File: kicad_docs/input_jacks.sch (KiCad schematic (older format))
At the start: 32 parts, among them J10 gate_3_in, J11 trigger_3_in, J12 gate_4_in, J13 trigger_4_in, J6 gate_1_i n, J7 trigger_1_in, J8 gate_2_in, J9 trigger_2_in, Q10 MMBT3904, Q11 MMBT3904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

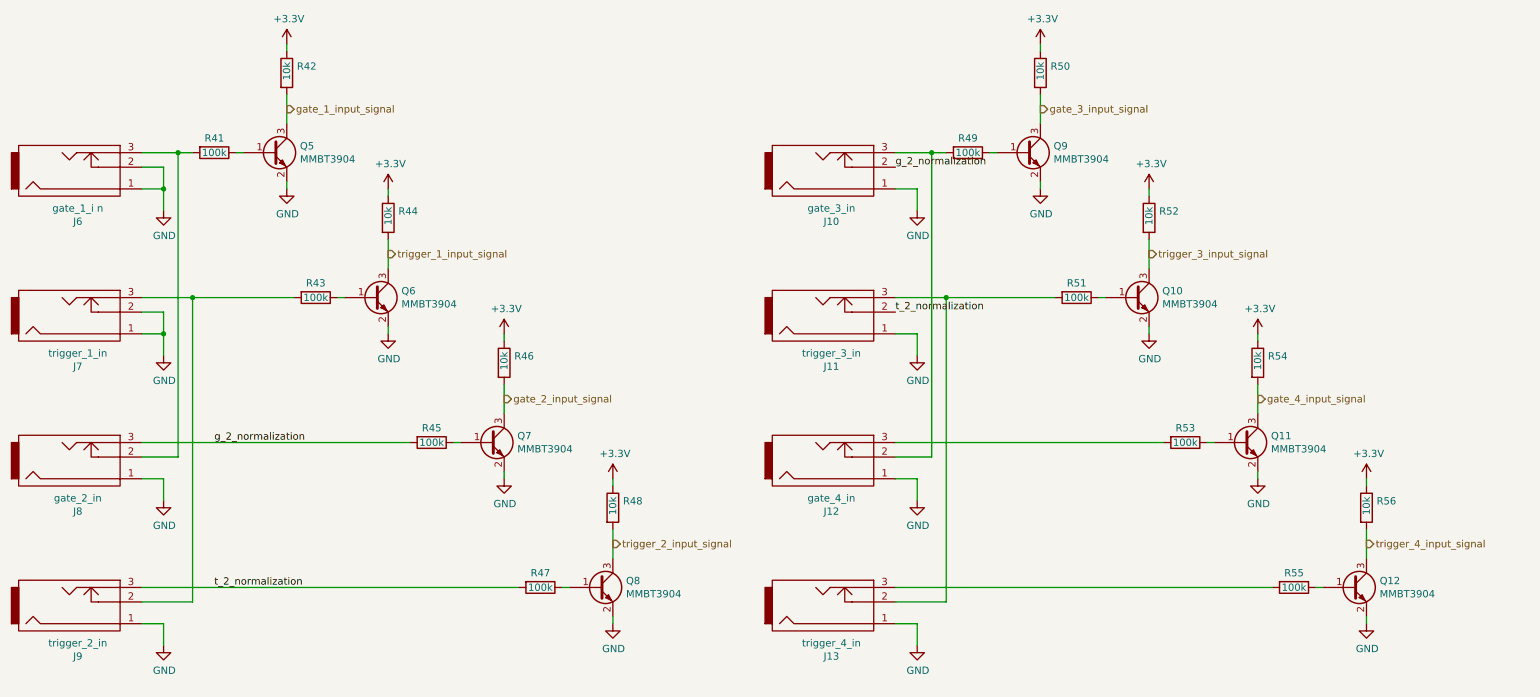
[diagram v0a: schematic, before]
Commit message: add EEPROM, big pcb re-design
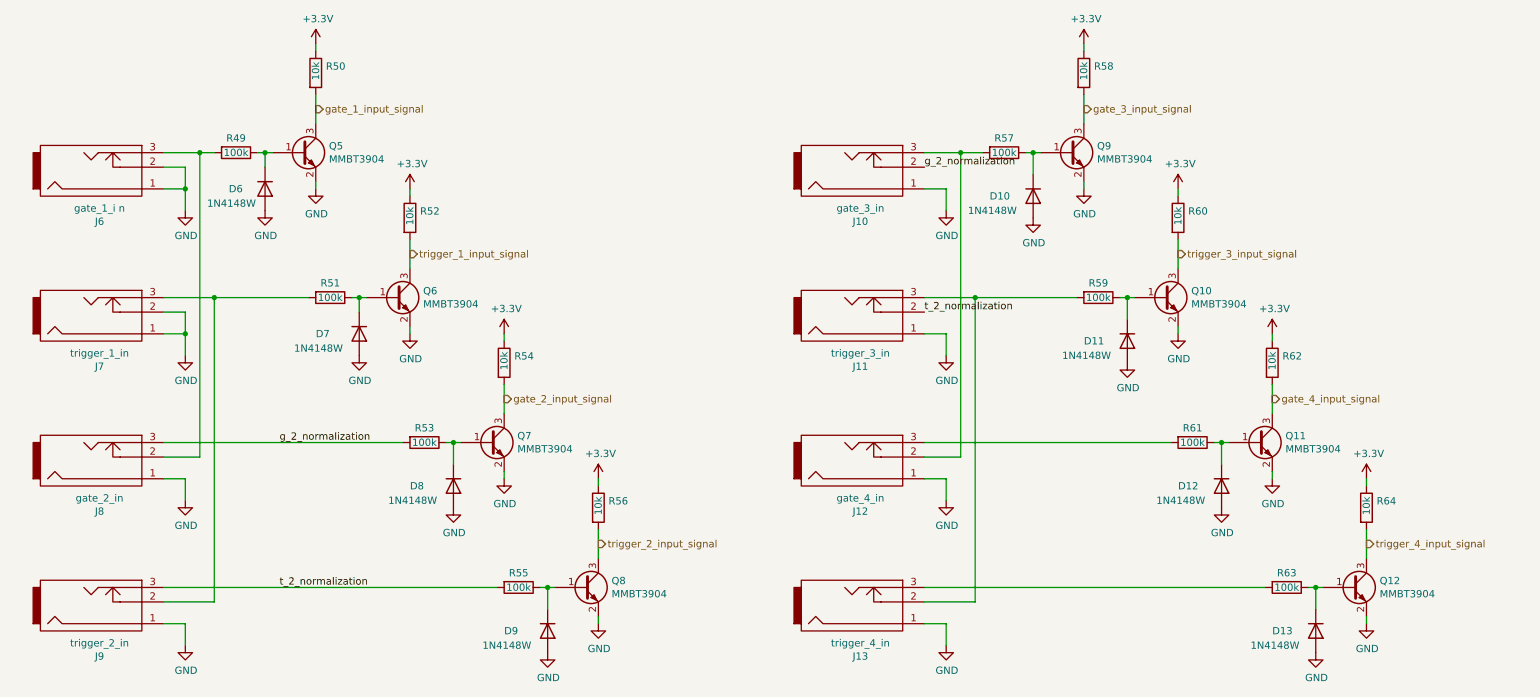
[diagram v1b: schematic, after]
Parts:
- added D10, D11, D12, D13, D6, D7, D8, D9: 1N4148W, Diode_SMD:D_SOD-123, symbol Diode:1N4148W
- Q10, Q11, Q12, Q5, Q6, Q7, Q8, Q9: footprint Package_TO_SOT_SMD:SOT-23_Handsoldering -> Package_TO_SOT_SMD:SOT-23
- R49: renamed from R41; footprint Resistor_SMD:R_0805_2012Metric_Pad1.15x1.40mm_HandSolder -> Resistor_SMD:R_0603_1608Metric
- R50: renamed from R42; footprint Resistor_SMD:R_0805_2012Metric_Pad1.15x1.40mm_HandSolder -> Resistor_SMD:R_0603_1608Metric
- R51: renamed from R43; footprint Resistor_SMD:R_0805_2012Metric_Pad1.15x1.40mm_HandSolder -> Resistor_SMD:R_0603_1608Metric
- R52: renamed from R44; footprint Resistor_SMD:R_0805_2012Metric_Pad1.15x1.40mm_HandSolder -> Resistor_SMD:R_0603_1608Metric
- R53: renamed from R45; footprint Resistor_SMD:R_0805_2012Metric_Pad1.15x1.40mm_HandSolder -> Resistor_SMD:R_0603_1608Metric
- R54: renamed from R46; footprint Resistor_SMD:R_0805_2012Metric_Pad1.15x1.40mm_HandSolder -> Resistor_SMD:R_0603_1608Metric
- R55: renamed from R47; footprint Resistor_SMD:R_0805_2012Metric_Pad1.15x1.40mm_HandSolder -> Resistor_SMD:R_0603_1608Metric
- R56: renamed from R48; footprint Resistor_SMD:R_0805_2012Metric_Pad1.15x1.40mm_HandSolder -> Resistor_SMD:R_0603_1608Metric
- R57: renamed from R49; footprint Resistor_SMD:R_0805_2012Metric_Pad1.15x1.40mm_HandSolder -> Resistor_SMD:R_0603_1608Metric
- R58: renamed from R50; footprint Resistor_SMD:R_0805_2012Metric_Pad1.15x1.40mm_HandSolder -> Resistor_SMD:R_0603_1608Metric
- R59: renamed from R51; footprint Resistor_SMD:R_0805_2012Metric_Pad1.15x1.40mm_HandSolder -> Resistor_SMD:R_0603_1608Metric
- R60: renamed from R52; footprint Resistor_SMD:R_0805_2012Metric_Pad1.15x1.40mm_HandSolder -> Resistor_SMD:R_0603_1608Metric
- R61: renamed from R53; footprint Resistor_SMD:R_0805_2012Metric_Pad1.15x1.40mm_HandSolder -> Resistor_SMD:R_0603_1608Metric
- R62: renamed from R54; footprint Resistor_SMD:R_0805_2012Metric_Pad1.15x1.40mm_HandSolder -> Resistor_SMD:R_0603_1608Metric
- R63: renamed from R55; footprint Resistor_SMD:R_0805_2012Metric_Pad1.15x1.40mm_HandSolder -> Resistor_SMD:R_0603_1608Metric
- R64: renamed from R56; footprint Resistor_SMD:R_0805_2012Metric_Pad1.15x1.40mm_HandSolder -> Resistor_SMD:R_0603_1608Metric
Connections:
- net GND: now also D10.2 (A), D11.2 (A), D12.2 (A), D13.2 (A), D6.2 (A), D7.2 (A), D8.2 (A), D9.2 (A)
- net at Q5.1 (B), R49.1: now also D6.1 (K)
- net at Q7.1 (B), R53.1: now also D8.1 (K)
- net at Q9.1 (B), R57.1: now also D10.1 (K)
- net at Q11.1 (B), R61.1: now also D12.1 (K)
- net at Q6.1 (B), R51.1: now also D7.1 (K)
- net at Q8.1 (B), R55.1: now also D9.1 (K)
- net at Q10.1 (B), R59.1: now also D11.1 (K)
- net at Q12.1 (B), R63.1: now also D13.1 (K)
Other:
- moved on the sheet: J10, J11, J12, J13, J6, J7, J8, J9, Q10, Q11, Q5, Q6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
